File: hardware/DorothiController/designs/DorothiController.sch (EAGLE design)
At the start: 25 parts

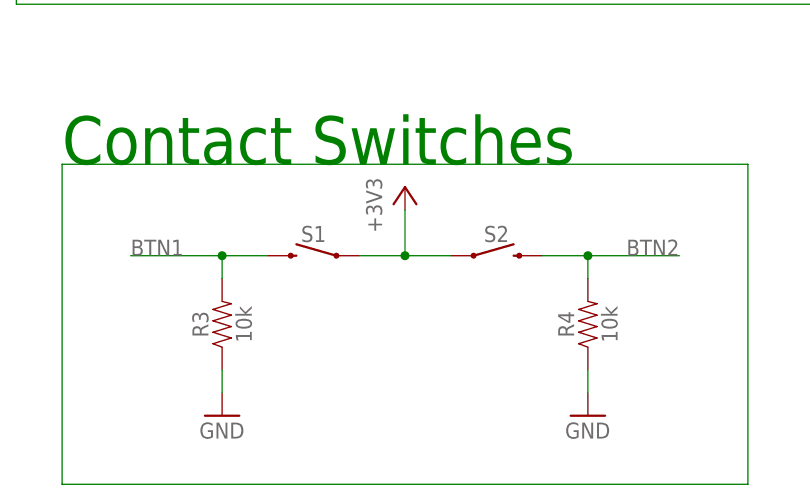
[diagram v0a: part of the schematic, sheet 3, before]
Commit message: general idea of board layout added
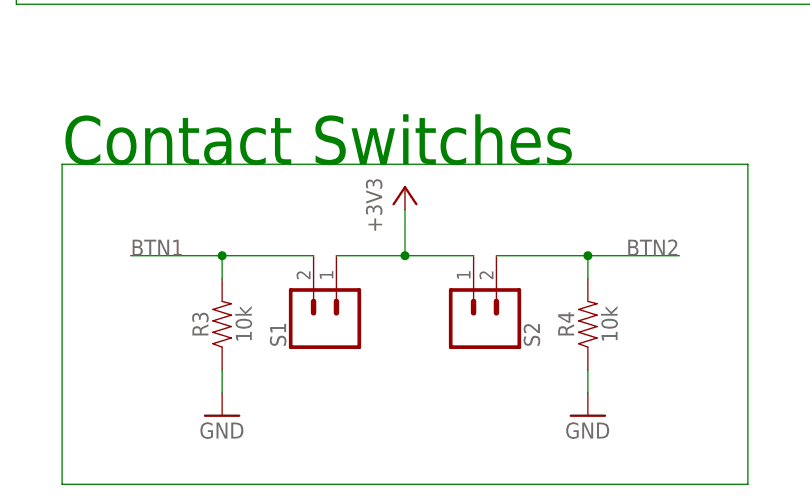
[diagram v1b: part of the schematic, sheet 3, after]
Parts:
- S1, S2: value MOMENTARY-SWITCH-SPST-PTH-12MM -> (none); device SparkFun-Switches:MOMENTARY-SWITCH-SPST-PTH-12MM -> SparkFun-Connectors:CONN_02
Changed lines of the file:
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@@
 <part name="+3V8" library="supply1" library_urn="urn:adsk.eagle:library:371" deviceset="+3V3" device=""/>
 <part name="GND11" library="supply1" library_urn="urn:adsk.eagle:library:371" deviceset="GND" device=""/>
-<part name="S1" library="SparkFun-Switches" library_urn="urn:adsk.eagle:library:535" deviceset="MOMENTARY-SWITCH-SPST" device="-PTH-12MM" package3d_urn="urn:adsk.eagle:package:40164/1" value=""/>
-<part name="S2" library="SparkFun-Switches" library_urn="urn:adsk.eagle:library:535" deviceset="MOMENTARY-SWITCH-SPST" device="-PTH-12MM" package3d_urn="urn:adsk.eagle:package:40164/1" value=""/>
 <part name="GND12" library="supply1" library_urn="urn:adsk.eagle:library:371" deviceset="GND" device=""/>
 <part name="R3" library="SparkFun-Resistors" library_urn="urn:adsk.eagle:library:532" deviceset="10KOHM" device="-0603-1/10W-1%" package3d_urn="urn:adsk.eagle:package:39650/1" value="10k"/>
@@
 <part name="GND15" library="supply1" library_urn="urn:adsk.eagle:library:371" deviceset="GND" device=""/>
 <part name="P+2" library="supply1" library_urn="urn:adsk.eagle:library:371" deviceset="+12V" device=""/>
+<part name="S1" library="SparkFun-Connectors" library_urn="urn:adsk.eagle:library:513" deviceset="CONN_02" device="" package3d_urn="urn:adsk.eagle:package:38039/1"/>
+<part name="S2" library="SparkFun-Connectors" library_urn="urn:adsk.eagle:library:513" deviceset="CONN_02" device="" package3d_urn="urn:adsk.eagle:package:38039/1"/>
 </parts>
 <sheets>
@@
 <attribute name="VALUE" x="208.28" y="71.12" size="1.778" layer="96"/>
 </instance>
-<instance part="S1" gate="G$1" x="76.2" y="88.9" smashed="yes" rot="MR0">
-<attribute name="NAME" x="76.2" y="90.424" size="1.778" layer="95" font="vector" rot="MR0" align="bottom-center"/>
-<attribute name="VALUE" x="76.2" y="88.392" size="1.778" layer="96" font="vector" rot="MR0" align="top-center"/>
-</instance>
-<instance part="S2" gate="G$1" x="96.52" y="88.9" smashed="yes">
-<attribute name="NAME" x="96.52" y="90.424" size="1.778" layer="95" font="vector" align="bottom-center"/>
-<attribute name="VALUE" x="96.52" y="88.392" size="1.778" layer="96" font="vector" align="top-center"/>
-</instance>
 <instance part="GND12" gate="1" x="66.04" y="71.12" smashed="yes">
 <attribute name="VALUE" x="63.5" y="68.58" size="1.778" layer="96"/>
@@
 <instance part="+3V9" gate="G$1" x="86.36" y="96.52" smashed="yes">
 <attribute name="VALUE" x="83.82" y="91.44" size="1.778" layer="96" rot="R90"/>
+</instance>
+<instance part="S1" gate="G$1" x="78.74" y="81.28" smashed="yes" rot="R90">
+<attribute name="VALUE" x="83.566" y="78.74" size="1.778" layer="96" font="vector" rot="R90"/>
+<attribute name="NAME" x="73.152" y="78.74" size="1.778" layer="95" font="vector" rot="R90"/>
+</instance>
+<instance part="S2" gate="G$1" x="93.98" y="81.28" smashed="yes" rot="MR90">
+<attribute name="VALUE" x="89.154" y="78.74" size="1.778" layer="96" font="vector" rot="MR90"/>
+<attribute name="NAME" x="99.568" y="78.74" size="1.778" layer="95" font="vector" rot="MR90"/>
 </instance>
 </instances>
@@
 </segment>
 <segment>
+<pinref part="+3V9" gate="G$1" pin="+3V3"/>
+<wire x1="86.36" y1="88.9" x2="86.36" y2="93.98" width="0.1524" layer="91"/>
+<pinref part="S1" gate="G$1" pin="1"/>
+<wire x1="78.74" y1="88.9" x2="86.36" y2="88.9" width="0.1524" layer="91"/>
 <pinref part="S2" gate="G$1" pin="1"/>
-<pinref part="S1" gate="G$1" pin="1"/>
-<wire x1="91.44" y1="88.9" x2="86.36" y2="88.9" width="0.1524" layer="91"/>
-<pinref part="+3V9" gate="G$1" pin="+3V3"/>
-<wire x1="86.36" y1="88.9" x2="81.28" y2="88.9" width="0.1524" layer="91"/>
-<wire x1="86.36" y1="88.9" x2="86.36" y2="93.98" width="0.1524" layer="91"/>
+<wire x1="86.36" y1="88.9" x2="93.98" y2="88.9" width="0.1524" layer="91"/>
 <junction x="86.36" y="88.9"/>
 </segment>
@@
 <net name="BTN1" class="0">
 <segment>
-<pinref part="S1" gate="G$1" pin="2"/>
-<wire x1="71.12" y1="88.9" x2="66.04" y2="88.9" width="0.1524" layer="91"/>
 <label x="55.88" y="88.9" size="1.778" layer="95"/>
 <pinref part="R3" gate="G$1" pin="2"/>
 <wire x1="66.04" y1="88.9" x2="55.88" y2="88.9" width="0.1524" layer="91"/>
 <wire x1="66.04" y1="86.36" x2="66.04" y2="88.9" width="0.1524" layer="91"/>
+<pinref part="S1" gate="G$1" pin="2"/>
+<wire x1="76.2" y1="88.9" x2="66.04" y2="88.9" width="0.1524" layer="91"/>
 <junction x="66.04" y="88.9"/>
 </segment>
@@
 <net name="BTN2" class="0">
 <segment>
-<pinref part="S2" gate="G$1" pin="2"/>
-<wire x1="101.6" y1="88.9" x2="106.68" y2="88.9" width="0.1524" layer="91"/>
 <label x="116.84" y="88.9" size="1.778" layer="95" align="bottom-right"/>
 <pinref part="R4" gate="G$1" pin="2"/>
 <wire x1="106.68" y1="88.9" x2="116.84" y2="88.9" width="0.1524" layer="91"/>
 <wire x1="106.68" y1="86.36" x2="106.68" y2="88.9" width="0.1524" layer="91"/>
+<pinref part="S2" gate="G$1" pin="2"/>
+<wire x1="96.52" y1="88.9" x2="106.68" y2="88.9" width="0.1524" layer="91"/>
 <junction x="106.68" y="88.9"/>
 </segment>

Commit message: controller ready
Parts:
- C1: value 0.1uF -> 10uF; device SparkFun-Capacitors:0.1UF-0603-25V-5% -> SparkFun-Capacitors:10UF-POLAR-EIA3528-20V-10%(TANT)
- C4: value 10uF -> 0.1uF; device SparkFun-Capacitors:10UF-POLAR-EIA3528-20V-10%(TANT) -> SparkFun-Capacitors:0.1UF-0603-25V-5%
- TB1: device TB6612FNG:TB6612FNG -> TB6612FNG:TB6612FNG(O,C,8,EL
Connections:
- net N$6 renamed 5V_OUT
- net +12V: now also C3.+, C4.1, TB1.VM1, TB1.VM2, TB1.VM3; no longer C2.1, C4.+, TB1.VM
- net +3V3: now also C1.+, C2.1, LINE1.3; no longer C1.1, C3.+, LINE1.2
- net GND: now also C1.-, C4.2, LINE1.4, TB1.GND, TB1.PGND1@1, TB1.PGND1@2, TB1.PGND2@1, TB1.PGND2@2; no longer C1.2, C4.-, LINE1.1, TB1.GND1, TB1.GND2, TB1.GND3
- net IMU_INT1: now also U$1.13/SCK0/LED; no longer U$1.35/A16/PWM
- net IMU_INT2: now also U$1.39/A20; no longer U$1.36/A17/PWM
- net LINE1_RS1: now also LINE1.1, U$1.10/TX2/PWM; no longer LINE1.3, U$1.12/MISO0
- net LINE1_RS2: now also LINE1.2, U$1.11/MOSI0; no longer LINE1.4, U$1.13/SCK0/LED
- net MA+: now also TB1.AO1@1, TB1.AO1@2; no longer TB1.A1
- net MA-: now also TB1.AO2@1, TB1.AO2@2; no longer TB1.A2
- net MB+: now also TB1.BO1@1, TB1.BO1@2; no longer TB1.B1
- net MB-: now also TB1.BO2@1, TB1.BO2@2; no longer TB1.B2
- net M_AIN1: now also U$1.29/T/PWM; no longer U$1.28
- net M_AIN2: now also U$1.28; no longer U$1.29/T/PWM
- net M_BIN1: now also U$1.31/A12/RX4; no longer U$1.30/T/PWM
- net M_BIN2: now also U$1.32/A13/TX4; no longer U$1.31/A12/RX4
- net M_PWMA: now also U$1.16/A2/T/PWM; no longer U$1.22/A8/T/PWM
- net M_PWMB: now also U$1.35/A16/PWM; no longer U$1.23/A9/T/PWM
- net M_STBY: now also U$1.30/T/PWM; no longer U$1.32/A13/TX4
- net TOF1_READY: now also U$1.20/A6/PWM; no longer U$1.17/A3/T/PWM
- net TOF1_SHDN: now also U$1.21/A7/PWM; no longer U$1.20/A6/PWM
- net TOF2_SHDN: now also U$1.1/TX1/MISO1/T; no longer U$1.5/PWM
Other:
- moved on the sheet: C2, C3, MA+, MA-, MB+, MB-
